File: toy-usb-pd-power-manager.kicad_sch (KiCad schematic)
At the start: 169 parts, among them J1 USB_C_2_0, J2 PINS_LHS, J3 PINS_RHS, Q1 Si7223DN, Q2 Si7224DN, Q3 Si7224DN, Q4 Si7224DN, Q5 Si7223DN, Q6 BSS138PS, Q7 BSS138PS, Q8 BSS138PS, U1 HUSB238_002DD, U2 BQ25672, U3 MAX17205G, U4 TPS63070, U5 TPS7A2601DRVR

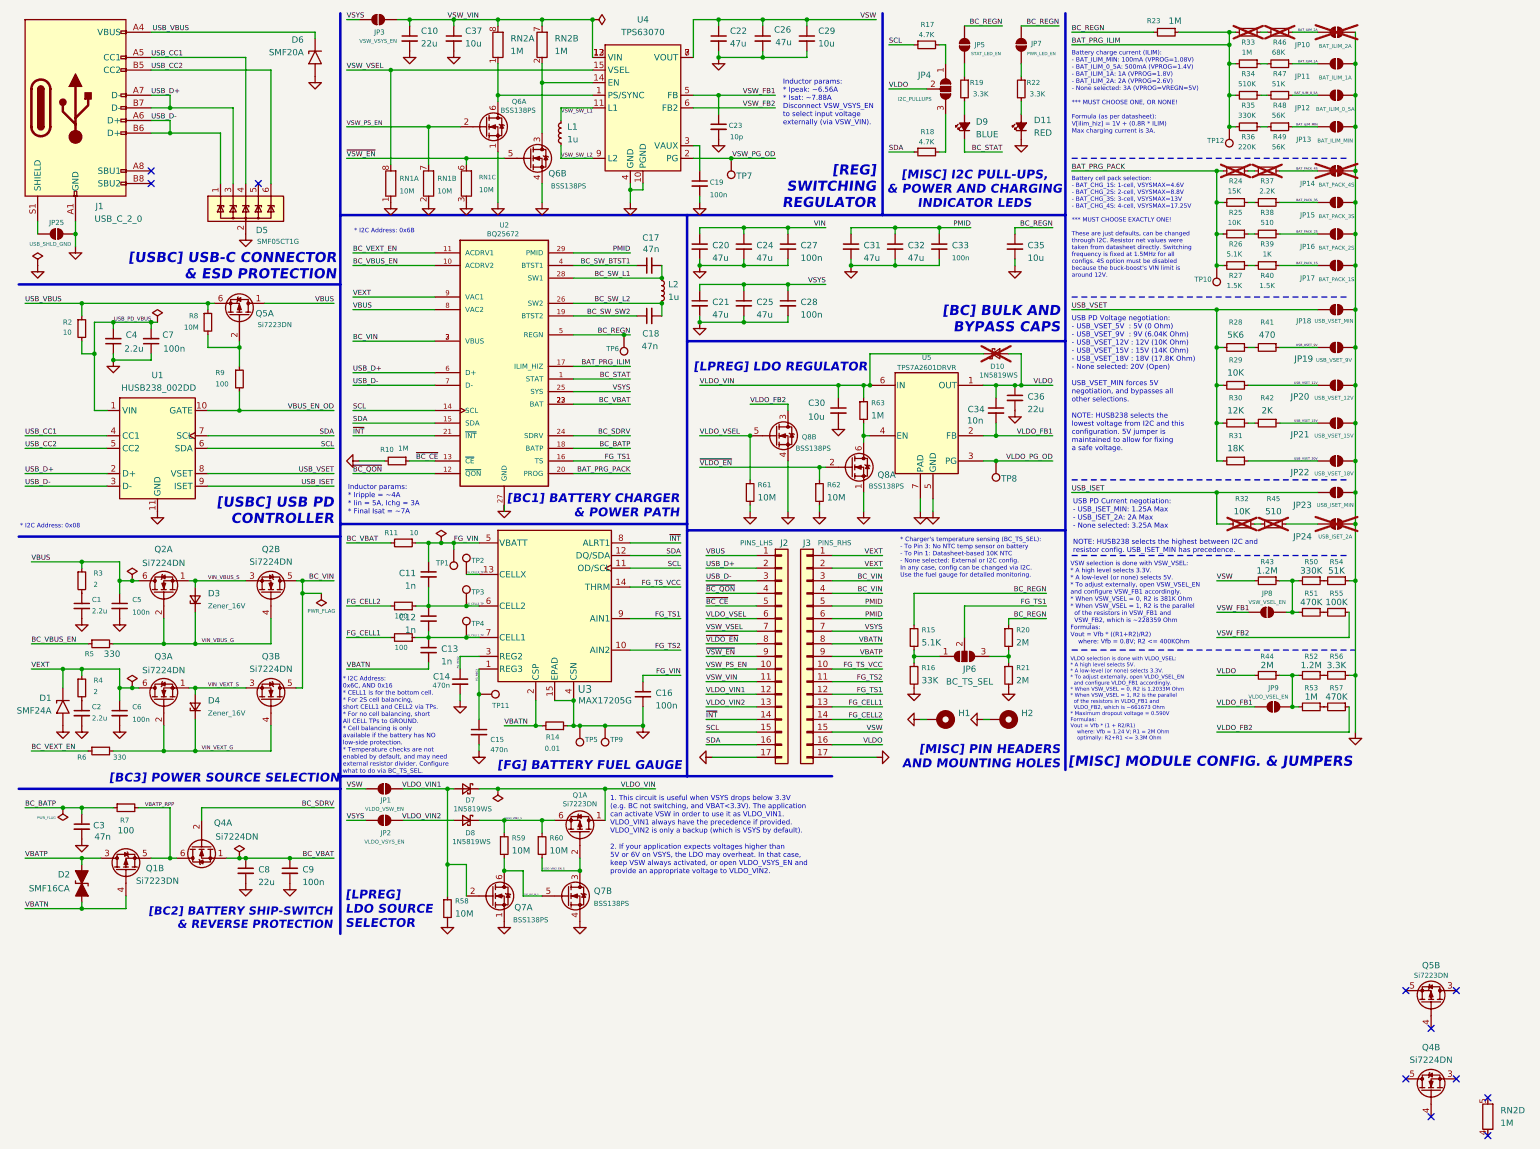
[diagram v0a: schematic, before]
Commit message: refactor(pcb): improve positioning of ICs on the board
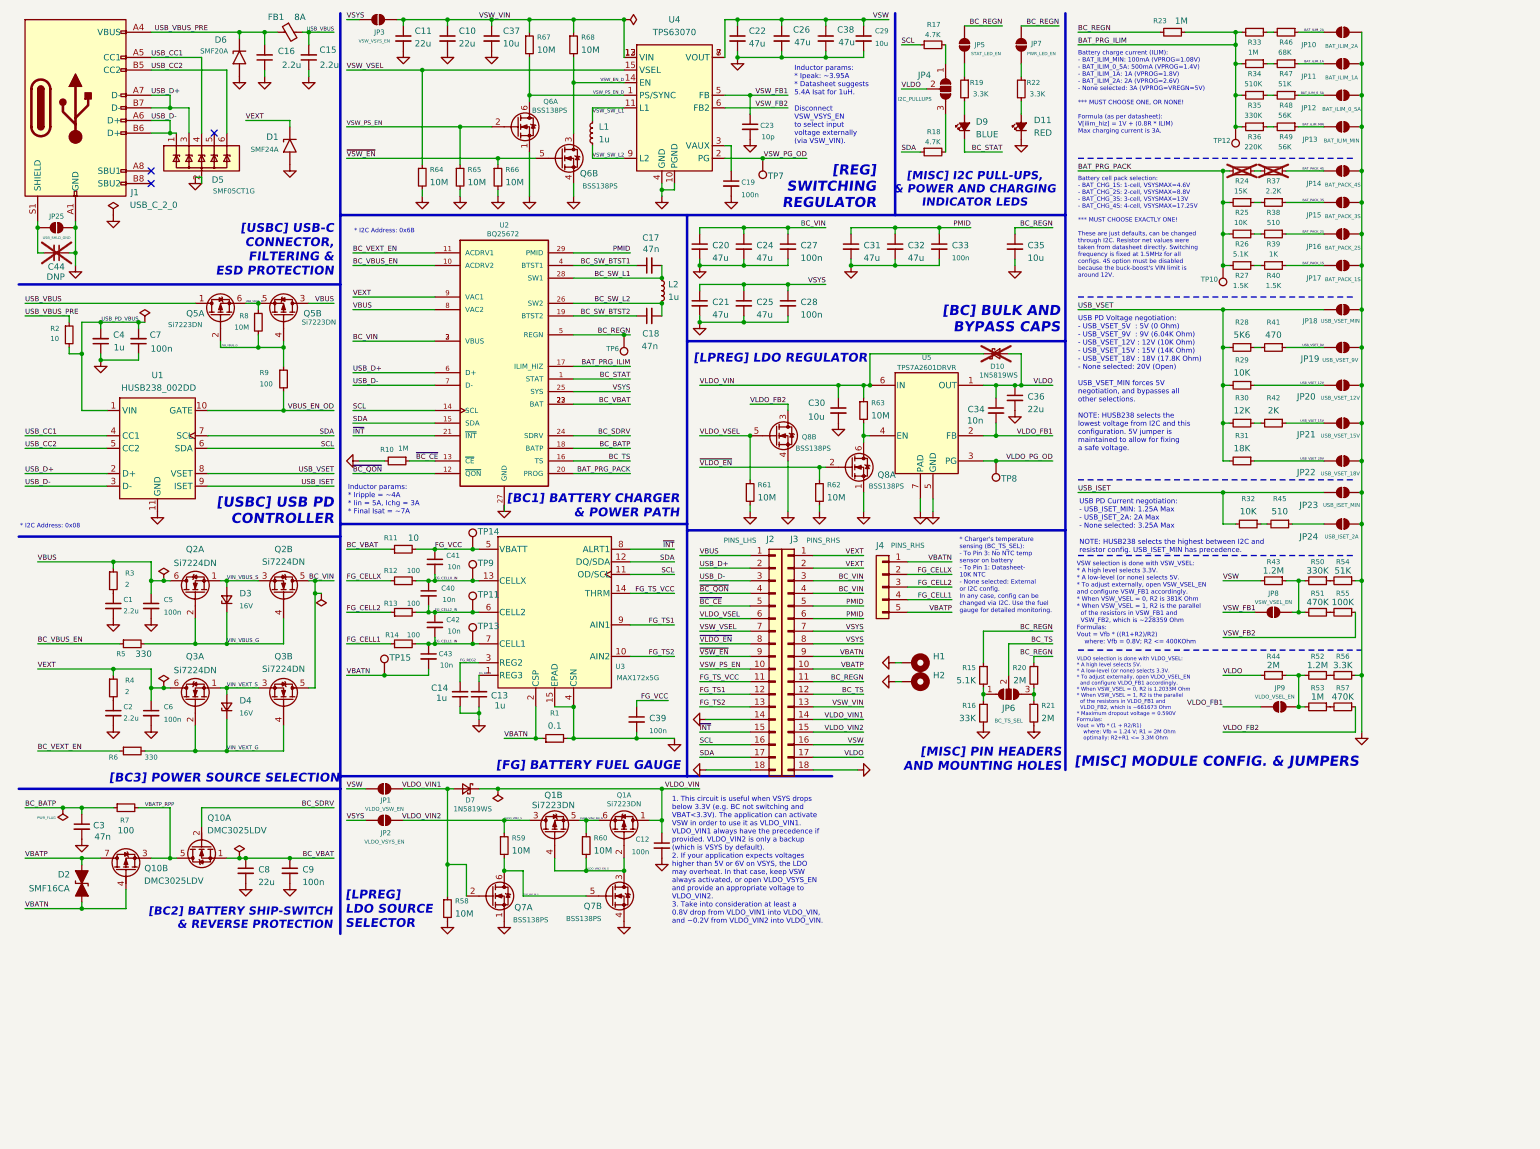
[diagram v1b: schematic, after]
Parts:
- removed D8: 1N5819WS, Diode_SMD:D_SOD-323, symbol Device:D_Schottky_Small
- removed Q4: Si7224DN, Package_SO:Vishay_PowerPAK_1212-8_Dual, symbol mixlib-discrete-mosfet:Si7224DN
- removed RN1: 10M, Resistor_SMD:R_Array_Convex_4x0603, symbol Device:R_Pack04_Split
- removed RN2: 1M, Resistor_SMD:R_Array_Concave_4x0603, symbol Device:R_Pack04_Split
- removed TP1, TP2, TP3, TP4, TP5: TestPoint, TestPoint:TestPoint_Pad_1.0x1.0mm, symbol Connector:TestPoint
- added C38: 47u, Capacitor_SMD:C_0805_2012Metric, symbol Device:C_Small
- added C39: 100n, Capacitor_SMD:C_0402_1005Metric, symbol Device:C_Small
- added C40, C41, C42, C43: 10n, Capacitor_SMD:C_0402_1005Metric, symbol Device:C_Small
- added C44: DNP, Capacitor_SMD:C_0603_1608Metric, symbol Device:C_Small
- added FB1: 8A, Inductor_SMD:L_1210_3225Metric, symbol Device:FerriteBead_Small
- added J4: PINS_RHS, Connector_PinHeader_2.54mm:PinHeader_1x05_P2.54mm_Vertical, symbol Connector_Generic:Conn_01x05
- added Q10: DMC3025LDV, mixlib-generic-son:Diodes_PowerDI3333-8_UXC_3.3x3.3mm_P0.65mm, symbol mixlib-discrete-mosfet:DMC3025LDV
- added R1: 0.1, Resistor_SMD:R_1210_3225Metric, symbol Device:R_Small
- added R64, R65, R66, R67, R68: 10M, Resistor_SMD:R_0402_1005Metric, symbol Device:R_Small
- added TP13, TP14, TP15: TestPoint, TestPoint:TestPoint_Pad_1.0x1.0mm, symbol Connector:TestPoint
- C11: value 1n -> 22u; footprint Capacitor_SMD:C_0402_1005Metric -> Capacitor_SMD:C_0805_2012Metric
- C12: value 1n -> 100n
- C13: value 1n -> 1u
- C14: value 470n -> 1u
- C15: value 470n -> 2.2u; footprint Capacitor_SMD:C_0402_1005Metric -> Capacitor_SMD:C_0603_1608Metric
- C16: value 100n -> 2.2u; footprint Capacitor_SMD:C_0402_1005Metric -> Capacitor_SMD:C_0603_1608Metric
- C4: value 2.2u -> 1u; footprint Capacitor_SMD:C_0603_1608Metric -> Capacitor_SMD:C_0402_1005Metric
- D3, D4: value Zener_16V -> 16V
- J2, J3: footprint Connector_PinHeader_2.54mm:PinHeader_1x17_P2.54mm_Vertical -> Connector_PinHeader_2.54mm:PinHeader_1x18_P2.54mm_Vertical; symbol Connector_Generic:Conn_01x17 -> Connector_Generic:Conn_01x18
- JP10: footprint Jumper:SolderJumper-2_P1.3mm_Open_TrianglePad1.0x1.5mm -> Jumper:SolderJumper-2_P1.3mm_Open_Pad1.0x1.5mm; now fitted
- JP14, JP24: now fitted
- R11, R12, R13: footprint Resistor_SMD:R_0402_1005Metric -> Resistor_SMD:R_0603_1608Metric
- R14: value 0.01 -> 100; footprint Resistor_SMD:R_1210_3225Metric -> Resistor_SMD:R_0603_1608Metric
- R32, R45: footprint Resistor_SMD:R_0603_1608Metric -> Resistor_SMD:R_0402_1005Metric; now fitted; now in the parts list
- R33, R46: now fitted; now in the parts list
- R63: value 1M -> 10M
- U3: value MAX17205G -> MAX172x5G
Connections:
- net VIN is gone; now on net BC_VIN: C20.1, C24.1, C27.1
- net BC_REGN: now also J3.11 (Pin_11)
- net BC_SDRV: now also Q10.2 (G)
- net BC_VBAT: now also R11.1, Q10.1 (S); no longer R11.2
- net FG_CELL1: now also R14.1, J4.4 (Pin_4); no longer J3.13 (Pin_13), R13.2
- net FG_CELL2: now also R13.1, J4.3 (Pin_3); no longer J3.14 (Pin_14), R12.2
- net FG_REG2: now also C14.2; no longer C14.1
- net FG_REG3: now also C13.2; no longer C15.1, TP11.1
- net FG_TS1: now also J2.12 (Pin_12); no longer J3.12 (Pin_12), JP6.2 (C), U2.16 (TS)
- net FG_TS2: now also J2.13 (Pin_13); no longer J3.11 (Pin_11)
- net FG_TS_VCC: now also J2.11 (Pin_11); no longer J3.10 (Pin_10)
- net GND: now also C11.2, C12.2, C13.1, C14.1, C15.1, C16.1, J2.14 (Pin_14), J2.18 (Pin_18), J3.18 (Pin_18), C38.2, C39.2, C44.1, R1.2, R64.2, R65.2, R66.2; no longer C14.2, C15.2, C16.2, J2.17 (Pin_17), J3.17 (Pin_17), R14.1, TP9.1
- net SCL: now also J2.16 (Pin_16); no longer J2.15 (Pin_15)
- net SDA: now also J2.17 (Pin_17); no longer J2.16 (Pin_16)
- net USB_VBUS: now also C15.2, Q5.1 (D), FB1.2; no longer D6.1 (A1), J1.A4 (VBUS), J1.A9 (VBUS), J1.B4 (VBUS), J1.B9 (VBUS), Q5.6 (S), R2.1, R8.1
- net VBATN: now also J3.9 (Pin_9), C43.2, J4.1 (Pin_1), Q10.4 (G), R1.1, TP15.1; no longer C13.2, J3.8 (Pin_8), Q1.4 (G), R14.2
- net VBATP: now also J3.10 (Pin_10), J4.5 (Pin_5), Q10.7 (D); no longer J3.9 (Pin_9), Q1.3 (D)
- net VBATP_RPP: now also Q10.3 (S), Q10.5 (D); no longer Q1.5 (S)
- net VBUS: now also Q5.3 (D); no longer Q5.1 (D)
- net VLDO: now also J3.17 (Pin_17); no longer J3.16 (Pin_16)
- net VLDO_VIN: now also C12.1
- net VLDO_VIN1: now also J3.14 (Pin_14); no longer J2.12 (Pin_12)
- net VLDO_VIN2: now also J3.15 (Pin_15), Q1.3 (D), R59.1; no longer J2.13 (Pin_13)
- net VLDO_VIN2_EN_G: now also Q1.5 (S), Q1.6 (S), R60.1
- net VLDO_VIN2_EN_S: now also Q1.4 (G)
- net VSW: now also J3.16 (Pin_16), C38.1; no longer J3.15 (Pin_15)
- net VSW_PS_EN: now also R65.1
- net VSW_VIN: now also C11.1, J3.13 (Pin_13), R67.1, R68.1; no longer J2.11 (Pin_11)
- net VSW_VSEL: now also R64.1
- net VSYS: now also J3.8 (Pin_8)
- net ~{INT}: now also J2.15 (Pin_15); no longer J2.14 (Pin_14)
- net ~{VSW_EN}: now also R66.1
- net VSW_PS_EN_D: now reaches Q6.6 (D), U4.1 (PS/SYNC)
- net VSW_PS_EN_D: now also R67.2
- net VSW_EN_D: now reaches Q6.3 (D), U4.14 (EN)
- net VSW_EN_D: now also R68.2
- net at J1.S1 (SHIELD), JP25.1 (A): now also C44.2
- net USB_VBUS_G: now reaches Q5.4 (G)
- net USB_VBUS_G: now also Q5.2 (G), R8.2, R9.1
- net USB_VBUS_D: now reaches Q5.5 (S)
- net USB_VBUS_D: now also Q5.6 (S), R8.1
- net BC_SW_SW2 renamed BC_SW_BTST2
- removed net FG_CELL1_TP: C12.2, C13.1, R13.1, U3.7 (CELL1)
- removed net FG_CELL2_TP: C11.2, C12.1, R12.1, U3.6 (CELL2)
- net FG_CELLX_TP renamed FG_CELLX_IN
- net FG_CELLX_IN: now also R12.2, TP9.1, C40.1, C41.2
- removed net FG_VIN: C11.1, C16.1, R11.1, U3.5 (VBATT)
- removed net VLDO_VIN2_S: Q1.6 (S), R59.1, R60.1
- new net BC_TS: J3.12 (Pin_12), JP6.2 (C), U2.16 (TS)
- new net FG_CELL1_IN: C42.2, C43.1, R14.2, TP13.1, U3.7 (CELL1)
- new net FG_CELL2_IN: C40.2, C42.1, R13.2, TP11.1, U3.6 (CELL2)
- new net FG_CELLX: J4.2 (Pin_2), R12.1
- new net FG_VCC: C39.1, C41.1, R11.2, TP14.1, U3.5 (VBATT)
- new net USB_VBUS_PRE: C16.2, D6.1 (A1), FB1.1, J1.A4 (VBUS), J1.A9 (VBUS), J1.B4 (VBUS), J1.B9 (VBUS), R2.1
- no-connect marks 11 -> 3
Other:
- note added: "* Charger's temperature sensing (BC_TS_SEL): - To Pin 3: No NTC temp sensor on battery - To Pin 1: Datasheet- 10K NTC - None selected: External or I2C config. In any case, config can be changed via I2C. Use the fuel gauge for detailed monitoring."
- note added: "1. This circuit is useful when VSYS drops below 3.3V (e.g. BC not switching and VBAT<3.3V). The application can activate VSW in order to use it as VLDO_VIN1. VLDO_VIN1 always have the precedence if provided. VLDO_VIN2 is only a backup (which is VSYS by default). 2. If your application expects voltages higher than 5V or 6V on VSYS, the LDO may overheat. In that case, keep VSW always activated, or 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"
- note added: "Inductor params: * Ipeak: ~3.95A * Datasheet suggests 5.4A Isat for 1uH. Disconnectr VSW_VSYS_ENr to select inputr voltage externallyr (via VSW_VIN)."
- note added: "[USBC] USB-C CONNECTOR, FILTERING & ESD PROTECTION"
- note removed: "* Charger's temperature sensing (BC_TS_SEL): - To Pin 3: No NTC temp sensor on battery - To Pin 1: Datasheet-based 10K NTC - None selected: External or I2C config. In any case, config can be changed via I2C. Use the fuel gauge for detailed monitoring."
- note removed: "* I2C Address: 0x6C, AND 0x16 * CELL1 is for the bottom cell. * For 2S cell balancing, short CELL1 and CELL2 via TPs. * For no cell balancing, short All CELL TPs to GROUND. * Cell balancing is only available if the battery has NO low-side protection. * Temperature checks are not enabled by default, and may need external resistor divider. Configure what to do via BC_TS_SEL."
- note removed: "1. This circuit is useful when VSYS drops below 3.3V (e.g. BC not switching, and VBAT<3.3V). The application can activate VSW in order to use it as VLDO_VIN1. VLDO_VIN1 always have the precedence if provided. VLDO_VIN2 is only a backup (which is VSYS by default). 2. If your application expects voltages higher than 5V or 6V on VSYS, the LDO may overheat. In that case, keep VSW always activated, or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"
- note removed: "Inductor params: * Ipeak: ~6.56A * Isat: ~7.88A Disconnect VSW_VSYS_EN to select input voltage externally (via VSW_VIN)."
- note removed: "[USBC] USB-C CONNECTOR & ESD PROTECTION"
- moved on the sheet: C1, C10, C19, C2, C22, C23, C26, C29, C37, C4, C5, C6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
